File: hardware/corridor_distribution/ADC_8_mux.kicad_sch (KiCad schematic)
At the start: 8 parts, among them CN1 C_Pack04_Split, U5 ADS7830

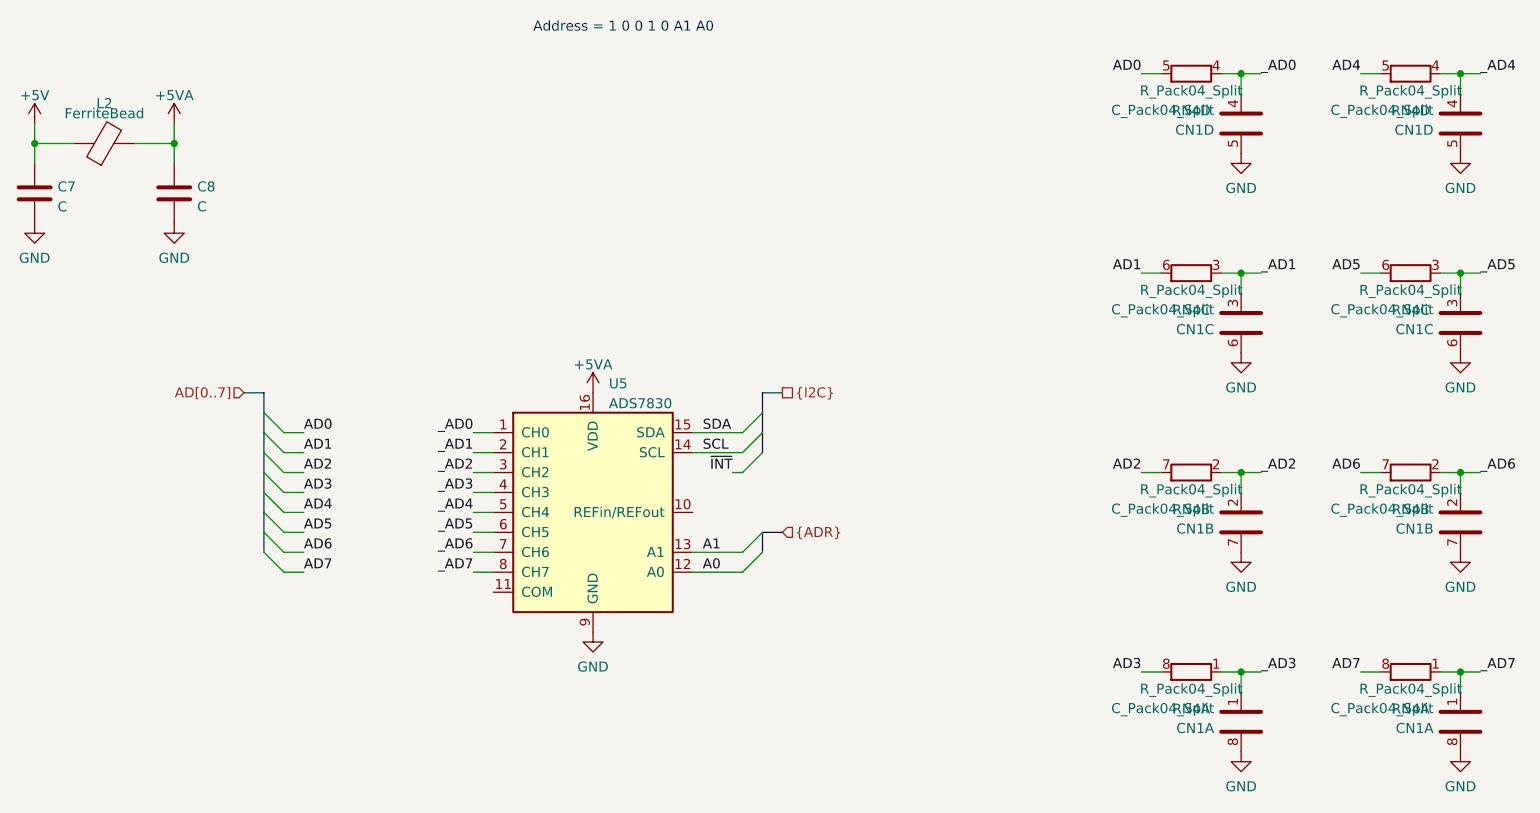
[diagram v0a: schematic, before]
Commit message: led balance and corridor ready
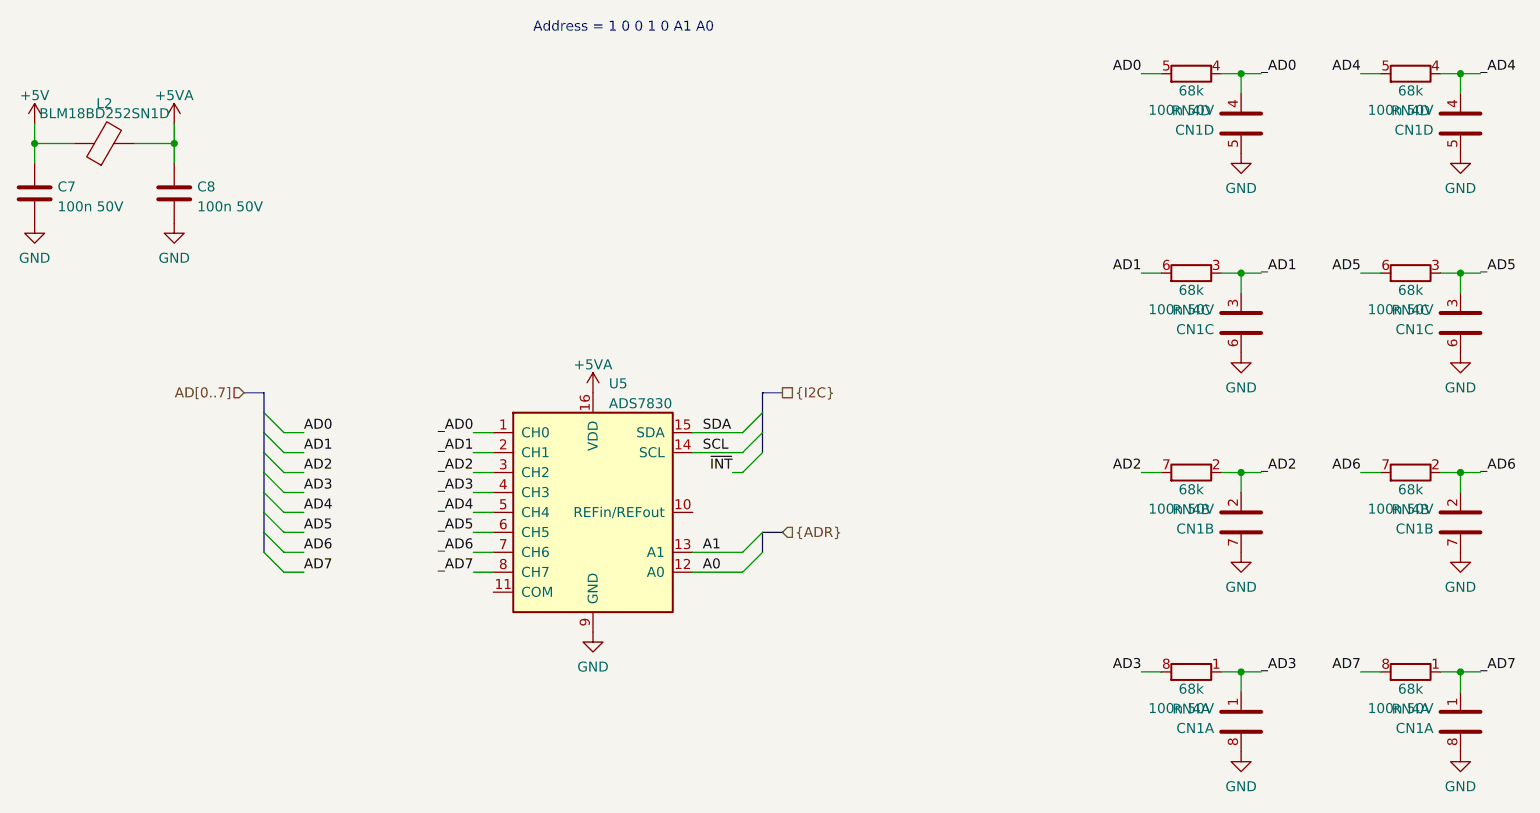
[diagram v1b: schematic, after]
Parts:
- C7, C8: value C -> 100n 50V; LCSC Part # (none) -> C14663; Total quantity (none) -> 30
- CN1: value C_Pack04_Split -> 100n 50V; LCSC Part # (none) -> C541605; Total quantity (none) -> 10
- L2: value FerriteBead -> BLM18BD252SN1D; LCSC Part # (none) -> C77668; Total quantity (none) -> 5
- RN4: value R_Pack04_Split -> 68k; LCSC Part # (none) -> C728919; Total quantity (none) -> 10
- U5: LCSC Part # (none) -> C161747; Total quantity (none) -> 5

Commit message: various
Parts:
- added C15: 100n 50V, Capacitor_SMD:C_0603_1608Metric, symbol Device:C
- added JP5: SolderJumper_2_Open, Jumper:SolderJumper-2_P1.3mm_Open_RoundedPad1.0x1.5mm, symbol Jumper:SolderJumper_2_Open
- added R17: R, Resistor_SMD:R_0603_1608Metric_Pad0.98x0.95mm_HandSolder, symbol Device:R
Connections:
- net +5VA: now also JP5.1 (A)
- net GND: now also U5.11 (COM), C15.2
- net _AD7: now also R17.2
- net REF: now reaches U5.10 (REFin/REFout)
- net REF: now also C15.1, JP5.2 (B)
- new net CS: R17.1
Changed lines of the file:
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@@
   (junction (at 189.23 39.37) (diameter 0) (color 0 0 0 0)
   )
+  (junction (at 148.59 95.25) (diameter 0) (color 0 0 0 0)
+  )
   (junction (at 217.17 115.57) (diameter 0) (color 0 0 0 0)
   )
@@
     (stroke (width 0) (type default))
   )
+  (wire (pts (xy 148.59 92.71) (xy 148.59 95.25))
+    (stroke (width 0) (type default))
+  )
   (bus (pts (xy 128.27 85.09) (xy 128.27 87.63))
     (stroke (width 0) (type default))
@@
     (stroke (width 0) (type default))
   )
+  (wire (pts (xy 148.59 95.25) (xy 148.59 97.79))
+    (stroke (width 0) (type default))
+  )
   (bus (pts (xy 64.77 82.55) (xy 64.77 80.01))
     (stroke (width 0) (type default))
   )
+  (wire (pts (xy 91.44 105.41) (xy 91.44 107.95))
+    (stroke (width 0) (type default))
+  )
   (wire (pts (xy 91.44 95.25) (xy 93.98 95.25))
     (stroke (width 0) (type default))
@@
     (stroke (width 0) (type default))
   )
+  (wire (pts (xy 146.05 95.25) (xy 148.59 95.25))
+    (stroke (width 0) (type default))
+  )
   (wire (pts (xy 125.73 102.87) (xy 119.38 102.87))
     (stroke (width 0) (type default))
@@
     (stroke (width 0) (type default))
   )
+  (wire (pts (xy 119.38 95.25) (xy 121.92 95.25))
+    (stroke (width 0) (type default))
+  )
   (bus (pts (xy 128.27 82.55) (xy 128.27 85.09))
     (stroke (width 0) (type default))
@@
     (stroke (width 0) (type default))
   )
+  (wire (pts (xy 93.98 105.41) (xy 91.44 105.41))
+    (stroke (width 0) (type default))
+  )
   (wire (pts (xy 217.17 39.37) (xy 219.71 39.37))
     (stroke (width 0) (type default))
@@
     (effects (font (size 1.27 1.27)) (justify left bottom))
   )
+  (label "REF" (at 121.92 95.25 0) (fields_autoplaced)
+    (effects (font (size 1.27 1.27)) (justify left bottom))
+  )
   (label "AD4" (at 204.47 39.37 180) (fields_autoplaced)
     (effects (font (size 1.27 1.27)) (justify right bottom))
   )
+  (label "REF" (at 146.05 95.25 180) (fields_autoplaced)
+    (effects (font (size 1.27 1.27)) (justify right bottom))
+  )
   (label "AD2" (at 69.85 90.17 0) (fields_autoplaced)
     (effects (font (size 1.27 1.27)) (justify left bottom))
@@
     (effects (font (size 1.27 1.27)) (justify right bottom))
   )
+  (label "_AD7" (at 109.22 50.8 0) (fields_autoplaced)
+    (effects (font (size 1.27 1.27)) (justify left bottom))
+  )
   (label "_AD1" (at 191.77 64.77 0) (fields_autoplaced)
     (effects (font (size 1.27 1.27)) (justify left bottom))
@@
   (label "_AD4" (at 219.71 39.37 0) (fields_autoplaced)
     (effects (font (size 1.27 1.27)) (justify left bottom))
+  )
+  (hierarchical_label "CS" (shape input) (at 101.6 50.8 180) (fields_autoplaced)
+    (effects (font (size 1.27 1.27)) (justify right))
   )
   (hierarchical_label "{ADR}" (shape input) (at 130.81 97.79 0) (fields_autoplaced)
@@
     )
   )
+  (symbol (lib_id "power:GND") (at 91.44 107.95 0) (unit 1)
+    (in_bom yes) (on_board yes) (dnp no) (fields_autoplaced)
+    (property "Reference" "#PWR068" (at 91.44 114.3 0)
+      (effects (font (size 1.27 1.27)) hide)
+    )
+    (property "Value" "GND" (at 91.44 112.3934 0)
+      (effects (font (size 1.27 1.27)))
+    )
+    (property "Footprint" "" (at 91.44 107.95 0)
+      (effects (font (size 1.27 1.27)) hide)
+    )
+    (property "Datasheet" "" (at 91.44 107.95 0)
+      (effects (font (size 1.27 1.27)) hide)
+    )
+    (pin "1")
+    (instances
+      (project "corridor_distribution"
+        (path "/d4c2f312-ca5d-462b-a371-0fb5d5a0cf93/3eb5a6aa-6213-4740-9488-5bd27eb25e70"
+          (reference "#PWR068") (unit 1)
+        )
+      )
+    )
+  )
+  (symbol (lib_id "power:+5VA") (at 148.59 85.09 0) (unit 1)
+    (in_bom yes) (on_board yes) (dnp no) (fields_autoplaced)
+    (property "Reference" "#PWR077" (at 148.59 88.9 0)
+      (effects (font (size 1.27 1.27)) hide)
+    )
+    (property "Value" "+5VA" (at 148.59 80.01 0)
+      (effects (font (size 1.27 1.27)))
+    )
+    (property "Footprint" "" (at 148.59 85.09 0)
+      (effects (font (size 1.27 1.27)) hide)
+    )
+    (property "Datasheet" "" (at 148.59 85.09 0)
+      (effects (font (size 1.27 1.27)) hide)
+    )
+    (pin "1")
+    (instances
+      (project "corridor_distribution"
+        (path "/d4c2f312-ca5d-462b-a371-0fb5d5a0cf93/3eb5a6aa-6213-4740-9488-5bd27eb25e70"
+          (reference "#PWR077") (unit 1)
+        )
+      )
+    )
+  )
   (symbol (lib_id "power:GND") (at 189.23 125.73 0) (mirror y) (unit 1)
     (in_bom yes) (on_board yes) (dnp no) (fields_autoplaced)
@@
         (path "/d4c2f312-ca5d-462b-a371-0fb5d5a0cf93/3eb5a6aa-6213-4740-9488-5bd27eb25e70"
           (reference "#PWR015") (unit 1)
+        )
+      )
+    )
+  )
+  (symbol (lib_id "Device:R") (at 105.41 50.8 90) (unit 1)
+    (in_bom yes) (on_board yes) (dnp no) (fields_autoplaced)
+    (property "Reference" "R17" (at 105.41 44.45 90)
+      (effects (font (size 1.27 1.27)))
+    )
+    (property "Value" "R" (at 105.41 46.99 90)
+      (effects (font (size 1.27 1.27)))
+    )
+    (property "Footprint" "Resistor_SMD:R_0603_1608Metric_Pad0.98x0.95mm_HandSolder" (at 105.41 52.578 90)
+      (effects (font (size 1.27 1.27)) hide)
+    )
+    (property "Datasheet" "~" (at 105.41 50.8 0)
+      (effects (font (size 1.27 1.27)) hide)
+    )
+    (pin "1")
+    (pin "2")
+    (instances
+      (project "corridor_distribution"
+        (path "/d4c2f312-ca5d-462b-a371-0fb5d5a0cf93/3eb5a6aa-6213-4740-9488-5bd27eb25e70"
+          (reference "R17") (unit 1)
         )
       )
@@
     )
   )
+  (symbol (lib_id "Jumper:SolderJumper_2_Open") (at 148.59 88.9 270) (unit 1)
+    (in_bom yes) (on_board yes) (dnp no) (fields_autoplaced)
+    (property "Reference" "JP5" (at 151.13 87.63 90)
+      (effects (font (size 1.27 1.27)) (justify left))
+    )
+    (property "Value" "SolderJumper_2_Open" (at 151.13 90.17 90)
+      (effects (font (size 1.27 1.27)) (justify left))
+    )
+    (property "Footprint" "Jumper:SolderJumper-2_P1.3mm_Open_RoundedPad1.0x1.5mm" (at 148.59 88.9 0)
+      (effects (font (size 1.27 1.27)) hide)
+    )
+    (property "Datasheet" "~" (at 148.59 88.9 0)
+      (effects (font (size 1.27 1.27)) hide)
+    )
+    (pin "1")
+    (pin "2")
+    (instances
+      (project "corridor_distribution"
+        (path "/d4c2f312-ca5d-462b-a371-0fb5d5a0cf93/cbc143e2-a435-47df-91fd-d639c7126821"
+          (reference "JP5") (unit 1)
+        )
+        (path "/d4c2f312-ca5d-462b-a371-0fb5d5a0cf93/3eb5a6aa-6213-4740-9488-5bd27eb25e70"
+          (reference "JP6") (unit 1)
+        )
+      )
+    )
+  )
   (symbol (lib_id "power:+5VA") (at 106.68 80.01 0) (unit 1)
     (in_bom yes) (on_board yes) (dnp no) (fields_autoplaced)
@@
     )
   )
+  (symbol (lib_id "power:GND") (at 148.59 105.41 0) (unit 1)
+    (in_bom yes) (on_board yes) (dnp no) (fields_autoplaced)
+    (property "Reference" "#PWR076" (at 148.59 111.76 0)
+      (effects (font (size 1.27 1.27)) hide)
+    )
+    (property "Value" "GND" (at 148.59 109.8534 0)
+      (effects (font (size 1.27 1.27)))
+    )
+    (property "Footprint" "" (at 148.59 105.41 0)
+      (effects (font (size 1.27 1.27)) hide)
+    )
+    (property "Datasheet" "" (at 148.59 105.41 0)
+      (effects (font (size 1.27 1.27)) hide)
+    )
+    (pin "1")
+    (instances
+      (project "corridor_distribution"
+        (path "/d4c2f312-ca5d-462b-a371-0fb5d5a0cf93/3eb5a6aa-6213-4740-9488-5bd27eb25e70"
+          (reference "#PWR076") (unit 1)
+        )
+      )
+    )
+  )
   (symbol (lib_id "Device:R_Pack04_Split") (at 210.82 64.77 90) (mirror x) (unit 3)
     (in_bom yes) (on_board yes) (dnp no) (fields_autoplaced)
@@
         )
       )
+    )
+  )
+  (symbol (lib_id "Device:C") (at 148.59 101.6 0) (unit 1)
+    (in_bom yes) (on_board yes) (dnp no) (fields_autoplaced)
+    (property "Reference" "C15" (at 151.511 100.7653 0)
+      (effects (font (size 1.27 1.27)) (justify left))
+    )
+    (property "Value" "100n 50V" (at 151.511 103.3022 0)
+      (effects (font (size 1.27 1.27)) (justify left))
+    )
+    (property "Footprint" "Capacitor_SMD:C_0603_1608Metric" (at 149.5552 105.41 0)
+      (effects (font (size 1.27 1.27)) hide)
+    )
+    (property "Datasheet" "~" (at 148.59 101.6 0)
+      (effects (font (size 1.27 1.27)) hide)
+    )
+    (property "LCSC Part #" "C14663" (at 148.59 101.6 0)
+      (effects (font (size 1.27 1.27)) hide)
+    )
+    (property "Total quantity" "30" (at 148.59 101.6 0)
+      (effects (font (size 1.27 1.27)) hide)
+    )
+    (pin "1")
+    (pin "2")
+    (instances
+      (project "corridor_distribution"
+        (path "/d4c2f312-ca5d-462b-a371-0fb5d5a0cf93/3eb5a6aa-6213-4740-9488-5bd27eb25e70"
+          (reference "C15") (unit 1)
+        )
+      )

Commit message: Night Light firmware
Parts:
- renumbered JP5 to JP6
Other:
- note added: "Address = _ 1 0 0 1 0 A1 A0 (0x48)"
- note removed: "Address = 1 0 0 1 0 A1 A0"
